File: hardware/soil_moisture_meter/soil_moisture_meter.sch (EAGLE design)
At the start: 16 parts, among them IC1 MEGA328, IC2 RFM12, IC3 74HC14D

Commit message: Remove battery measurement resistors.
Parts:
- removed R5: 100k, rcl:R-EU_R0603
- removed R6: 220R, rcl:R-EU_R0603
- R2: value 47k -> 220R
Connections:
- removed net N$1: IC1.PC1(ADC1/PCINT9), R3.2
- removed net N$14: IC1.PC0(ADC0/PCINT8), R2.2, R3.1
- net GND: no longer R2.1
- net N$10: now also R2.1; no longer R6.1
- net N$11: now also R2.2; no longer R6.2
- net N$2: now also R3.2; no longer R5.2
- net N$9: now also R3.1; no longer R5.1
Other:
- note added: "Date: 01.01.2015"
- note added: "Rev 1.1"
- note removed: "Date: 21.09.2014"
- note removed: "Rev 1.0"
- moved on the sheet: R2, R3
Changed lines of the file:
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@@
 <part name="P+2" library="supply1" deviceset="VCC" device=""/>
 <part name="P+3" library="supply1" deviceset="VCC" device=""/>
-<part name="GND3" library="supply1" deviceset="GND" device=""/>
 <part name="JP2" library="pinhead" deviceset="PINHD-1X1" device="" value="ANT"/>
 <part name="IC3" library="74xx-eu" deviceset="74*14" device="D" technology="HC"/>
-<part name="R2" library="rcl" deviceset="R-EU_" device="R0603" value="47k"/>
-<part name="R3" library="rcl" deviceset="R-EU_" device="R0603" value="100k"/>
 <part name="R1" library="rcl" deviceset="R-EU_" device="R0603" value="220R"/>
 <part name="R4" library="rcl" deviceset="R-EU_" device="R0603" value="1M"/>
-<part name="R5" library="rcl" deviceset="R-EU_" device="R0603" value="100k"/>
-<part name="R6" library="rcl" deviceset="R-EU_" device="R0603" value="220R"/>
+<part name="R3" library="rcl" deviceset="R-EU_" device="R0603" value="100k"/>
+<part name="R2" library="rcl" deviceset="R-EU_" device="R0603" value="220R"/>
 <part name="GND4" library="supply1" deviceset="GND" device=""/>
 <part name="GND5" library="supply1" deviceset="GND" device=""/>
@@
 <frame x1="-66.04" y1="-40.64" x2="154.94" y2="119.38" columns="8" rows="5" layer="97"/>
 <text x="63.5" y="104.14" size="3.81" layer="97">smarthomatic Soil Moisture Meter</text>
-<text x="114.3" y="99.06" size="2.1844" layer="97">Date: 21.09.2014</text>
-<text x="63.5" y="99.06" size="2.1844" layer="97">Rev 1.0</text>
+<text x="114.3" y="99.06" size="2.1844" layer="97">Date: 01.01.2015</text>
+<text x="63.5" y="99.06" size="2.1844" layer="97">Rev 1.1</text>
 <text x="63.5" y="93.98" size="2.1844" layer="97">Copyright (c) Uwe Freese, www.smarthomatic.org</text>
 <rectangle x1="33.02" y1="86.36" x2="38.1" y2="91.44" layer="97"/>
@@
 <instance part="P+2" gate="VCC" x="104.14" y="17.78" rot="R180"/>
 <instance part="P+3" gate="VCC" x="68.58" y="45.72" rot="R180"/>
-<instance part="GND3" gate="1" x="55.88" y="25.4"/>
 <instance part="JP2" gate="G$1" x="88.9" y="76.2"/>
 <instance part="IC3" gate="A" x="-22.86" y="76.2"/>
@@
 <instance part="IC3" gate="E" x="10.16" y="101.6"/>
 <instance part="IC3" gate="F" x="45.72" y="101.6"/>
-<instance part="R2" gate="G$1" x="55.88" y="35.56" rot="R90"/>
-<instance part="R3" gate="G$1" x="45.72" y="43.18" rot="R180"/>
 <instance part="R1" gate="G$1" x="58.42" y="5.08"/>
 <instance part="R4" gate="G$1" x="101.6" y="12.7" rot="R90"/>
-<instance part="R5" gate="G$1" x="-22.86" y="63.5"/>
-<instance part="R6" gate="G$1" x="63.5" y="71.12" rot="R270"/>
+<instance part="R3" gate="G$1" x="-22.86" y="63.5"/>
+<instance part="R2" gate="G$1" x="63.5" y="71.12" rot="R270"/>
 <instance part="GND4" gate="1" x="-38.1" y="93.98"/>
 <instance part="GND5" gate="1" x="60.96" y="12.7"/>
@@
 <junction x="127" y="-7.62"/>
 <pinref part="LED1" gate="G$1" pin="C"/>
-</segment>
-<segment>
-<pinref part="GND3" gate="1" pin="GND"/>
-<pinref part="R2" gate="G$1" pin="1"/>
-<wire x1="55.88" y1="27.94" x2="55.88" y2="30.48" width="0.1524" layer="91"/>
 </segment>
 <segment>
@@
 </segment>
 </net>
-<net name="N$14" class="0">
-<segment>
-<wire x1="55.88" y1="40.64" x2="55.88" y2="43.18" width="0.1524" layer="91"/>
-<pinref part="IC1" gate="1" pin="PC0(ADC0/PCINT8)"/>
-<wire x1="55.88" y1="43.18" x2="50.8" y2="43.18" width="0.1524" layer="91"/>
-<wire x1="35.56" y1="45.72" x2="55.88" y2="45.72" width="0.1524" layer="91"/>
-<wire x1="55.88" y1="45.72" x2="55.88" y2="43.18" width="0.1524" layer="91"/>
-<junction x="55.88" y="43.18"/>
-<pinref part="R2" gate="G$1" pin="2"/>
-<pinref part="R3" gate="G$1" pin="1"/>
-</segment>
-</net>
 <net name="N$16" class="0">
 <segment>
@@
 </segment>
 </net>
-<net name="N$1" class="0">
-<segment>
-<pinref part="IC1" gate="1" pin="PC1(ADC1/PCINT9)"/>
-<wire x1="35.56" y1="43.18" x2="40.64" y2="43.18" width="0.1524" layer="91"/>
-<pinref part="R3" gate="G$1" pin="2"/>
-</segment>
-</net>
 <net name="N$2" class="0">
 <segment>
@@
 <pinref part="IC3" gate="B" pin="I"/>
 <wire x1="-12.7" y1="76.2" x2="-5.08" y2="76.2" width="0.1524" layer="91"/>
-<pinref part="R5" gate="G$1" pin="2"/>
+<pinref part="R3" gate="G$1" pin="2"/>
 <wire x1="-5.08" y1="76.2" x2="0" y2="76.2" width="0.1524" layer="91"/>
 <wire x1="-17.78" y1="63.5" x2="-5.08" y2="63.5" width="0.1524" layer="91"/>
@@
 <wire x1="-38.1" y1="76.2" x2="-38.1" y2="63.5" width="0.1524" layer="91"/>
 <junction x="-38.1" y="76.2"/>
-<pinref part="R5" gate="G$1" pin="1"/>
+<pinref part="R3" gate="G$1" pin="1"/>
 <wire x1="-38.1" y1="63.5" x2="-27.94" y2="63.5" width="0.1524" layer="91"/>
 </segment>
@@
 <segment>
 <pinref part="IC3" gate="C" pin="O"/>
-<pinref part="R6" gate="G$1" pin="1"/>
+<pinref part="R2" gate="G$1" pin="1"/>
 <wire x1="55.88" y1="76.2" x2="63.5" y2="76.2" width="0.1524" layer="91"/>
 </segment>
@@
 <wire x1="35.56" y1="10.16" x2="63.5" y2="10.16" width="0.1524" layer="91"/>
 <wire x1="63.5" y1="10.16" x2="63.5" y2="66.04" width="0.1524" layer="91"/>
-<pinref part="R6" gate="G$1" pin="2"/>
-</segment>
-</net>
+<pinref part="R2" gate="G$1" pin="2"/>
+</segment>
+</net>

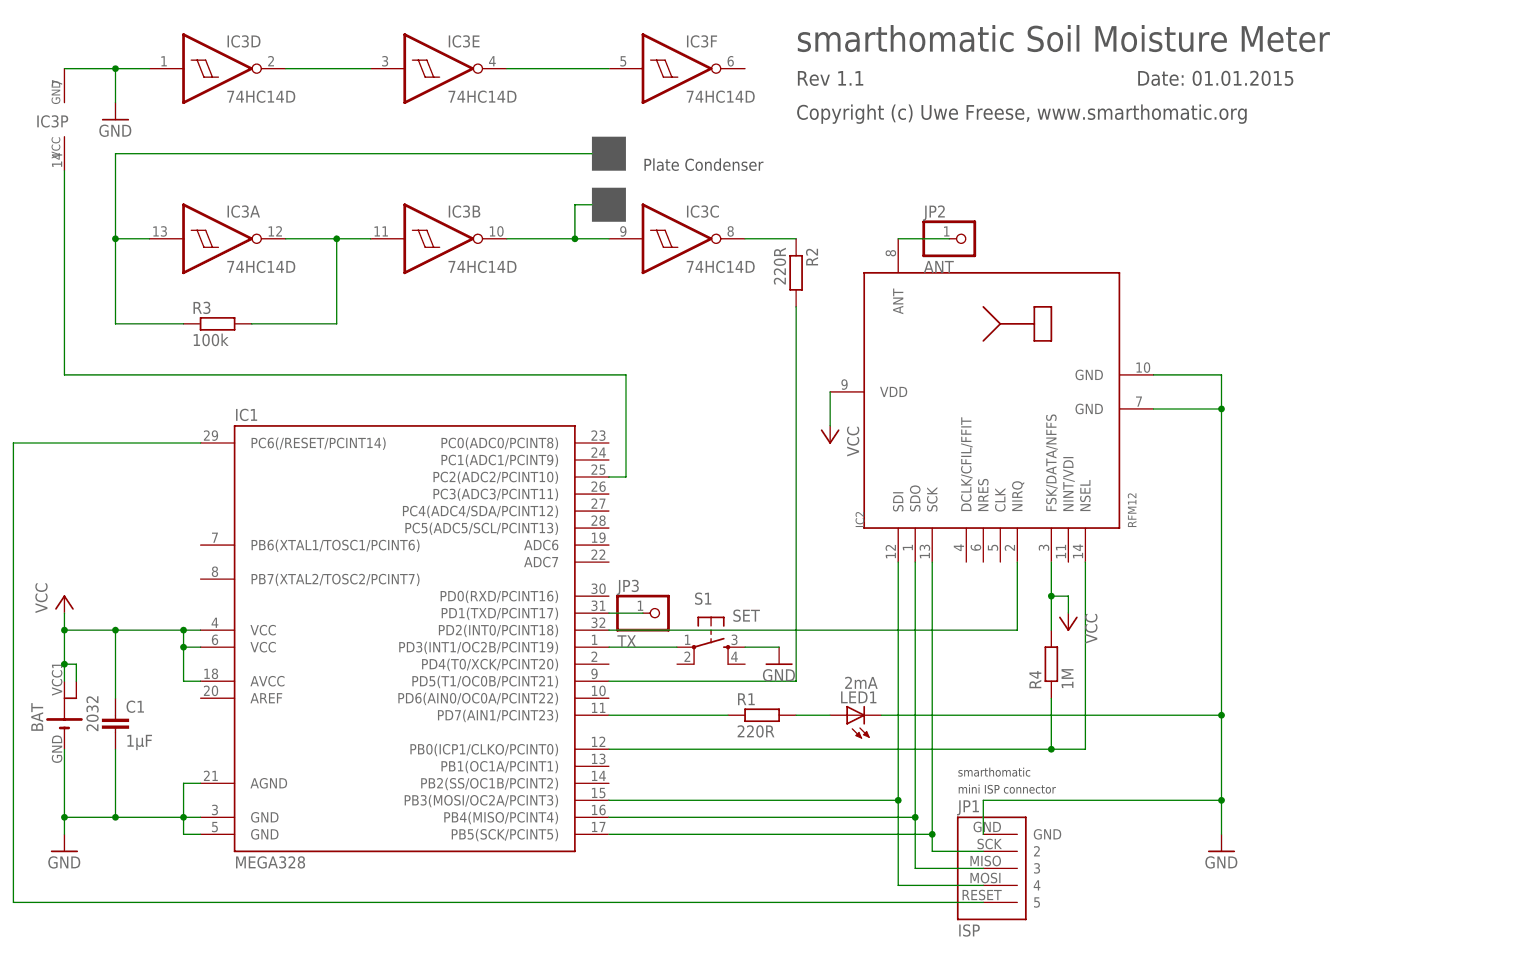
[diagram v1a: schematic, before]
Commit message: Change mini ISP connector and add 6th pin for VCC. Add solder jumper for VCC. Move ANT pin near RFM12B module. Remove resistor between 74GC14D and ATMega. Change LED resistor value.
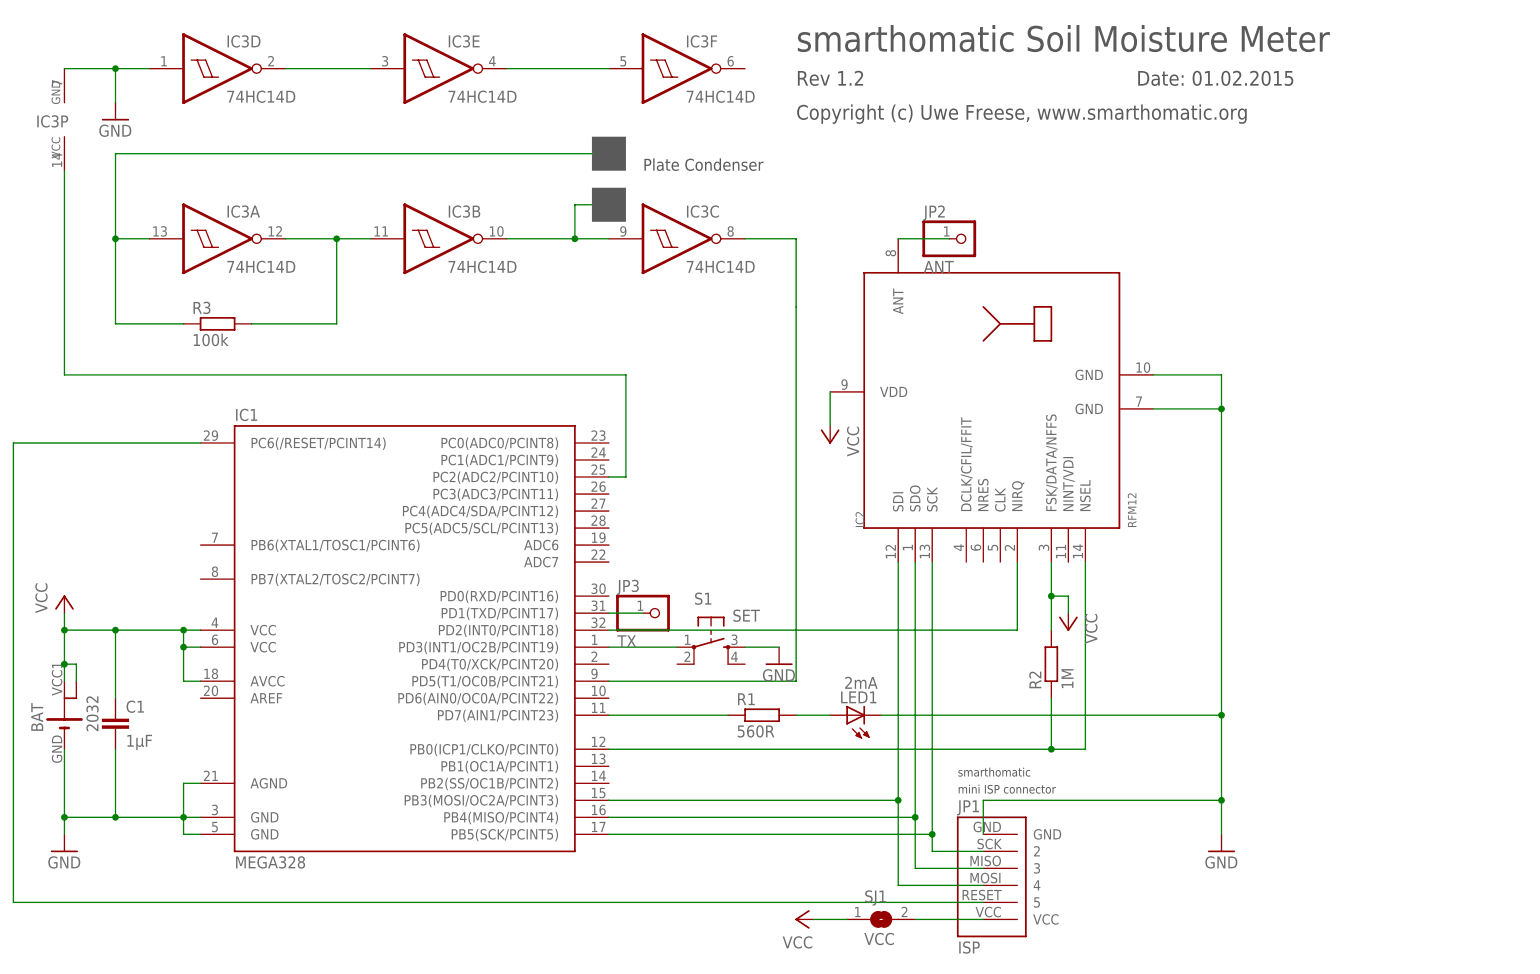
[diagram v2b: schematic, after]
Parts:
- removed R4: 1M, rcl:R-EU_R0603
- added SJ1: VCC, jumper:SJ
- R1: value 220R -> 560R
- R2: value 220R -> 1M
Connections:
- removed net N$11: IC1.PD5(T1/OC0B/PCINT21), R2.2
- new net N$1: JP1.VCC@6, SJ1.2
- net N$10: now also IC1.PD5(T1/OC0B/PCINT21); no longer R2.1
- net N$13: now also R2.1; no longer R4.1
- net VCC: now also R2.2, SJ1.1; no longer R4.2
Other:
- note added: "Date: 01.02.2015"
- note added: "Rev 1.2"
- note removed: "Date: 01.01.2015"
- note removed: "Rev 1.1"
- moved on the sheet: R2
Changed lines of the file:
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@@
 <grid distance="0.1" unitdist="inch" unit="inch" style="lines" multiple="1" display="no" altdistance="0.01" altunitdist="inch" altunit="inch"/>
 <layers>
-<layer number="1" name="Top" color="4" fill="1" visible="no" active="no"/>
-<layer number="16" name="Bottom" color="1" fill="1" visible="no" active="no"/>
-<layer number="17" name="Pads" color="2" fill="1" visible="no" active="no"/>
-<layer number="18" name="Vias" color="2" fill="1" visible="no" active="no"/>
-<layer number="19" name="Unrouted" color="6" fill="1" visible="no" active="no"/>
-<layer number="20" name="Dimension" color="15" fill="1" visible="no" active="no"/>
-<layer number="21" name="tPlace" color="7" fill="1" visible="no" active="no"/>
-<layer number="22" name="bPlace" color="7" fill="1" visible="no" active="no"/>
-<layer number="23" name="tOrigins" color="15" fill="1" visible="no" active="no"/>
-<layer number="24" name="bOrigins" color="15" fill="1" visible="no" active="no"/>
-<layer number="25" name="tNames" color="7" fill="1" visible="no" active="no"/>
-<layer number="26" name="bNames" color="7" fill="1" visible="no" active="no"/>
-<layer number="27" name="tValues" color="7" fill="1" visible="no" active="no"/>
-<layer number="28" name="bValues" color="7" fill="1" visible="no" active="no"/>
+<layer number="1" name="Top" color="4" fill="1" visible="yes" active="no"/>
+<layer number="16" name="Bottom" color="1" fill="1" visible="yes" active="no"/>
+<layer number="17" name="Pads" color="2" fill="1" visible="yes" active="no"/>
+<layer number="18" name="Vias" color="2" fill="1" visible="yes" active="no"/>
+<layer number="19" name="Unrouted" color="6" fill="1" visible="yes" active="no"/>
+<layer number="20" name="Dimension" color="15" fill="1" visible="yes" active="no"/>
+<layer number="21" name="tPlace" color="7" fill="1" visible="yes" active="no"/>
+<layer number="22" name="bPlace" color="7" fill="1" visible="yes" active="no"/>
+<layer number="23" name="tOrigins" color="15" fill="1" visible="yes" active="no"/>
+<layer number="24" name="bOrigins" color="15" fill="1" visible="yes" active="no"/>
+<layer number="25" name="tNames" color="7" fill="1" visible="yes" active="no"/>
+<layer number="26" name="bNames" color="7" fill="1" visible="yes" active="no"/>
+<layer number="27" name="tValues" color="7" fill="1" visible="yes" active="no"/>
+<layer number="28" name="bValues" color="7" fill="1" visible="yes" active="no"/>
 <layer number="29" name="tStop" color="7" fill="3" visible="no" active="no"/>
 <layer number="30" name="bStop" color="7" fill="6" visible="no" active="no"/>
@@
 <layer number="35" name="tGlue" color="7" fill="4" visible="no" active="no"/>
 <layer number="36" name="bGlue" color="7" fill="5" visible="no" active="no"/>
-<layer number="37" name="tTest" color="7" fill="1" visible="no" active="no"/>
-<layer number="38" name="bTest" color="7" fill="1" visible="no" active="no"/>
+<layer number="37" name="tTest" color="7" fill="1" visible="yes" active="no"/>
+<layer number="38" name="bTest" color="7" fill="1" visible="yes" active="no"/>
 <layer number="39" name="tKeepout" color="4" fill="11" visible="no" active="no"/>
 <layer number="40" name="bKeepout" color="1" fill="11" visible="no" active="no"/>
@@
 <layer number="44" name="Drills" color="7" fill="1" visible="no" active="no"/>
 <layer number="45" name="Holes" color="7" fill="1" visible="no" active="no"/>
-<layer number="46" name="Milling" color="3" fill="1" visible="no" active="no"/>
-<layer number="47" name="Measures" color="7" fill="1" visible="no" active="no"/>
-<layer number="48" name="Document" color="7" fill="1" visible="no" active="no"/>
-<layer number="49" name="Reference" color="7" fill="1" visible="no" active="no"/>
-<layer number="50" name="dxf" color="7" fill="1" visible="no" active="no"/>
-<layer number="51" name="tDocu" color="7" fill="1" visible="no" active="no"/>
-<layer number="52" name="bDocu" color="7" fill="1" visible="no" active="no"/>
+<layer number="46" name="Milling" color="3" fill="1" visible="yes" active="no"/>
+<layer number="47" name="Measures" color="7" fill="1" visible="yes" active="no"/>
+<layer number="48" name="Document" color="7" fill="1" visible="yes" active="no"/>
+<layer number="49" name="Reference" color="7" fill="1" visible="yes" active="no"/>
+<layer number="50" name="dxf" color="7" fill="1" visible="yes" active="no"/>
+<layer number="51" name="tDocu" color="7" fill="1" visible="yes" active="no"/>
+<layer number="52" name="bDocu" color="7" fill="1" visible="yes" active="no"/>
 <layer number="91" name="Nets" color="2" fill="1" visible="yes" active="yes"/>
 <layer number="92" name="Busses" color="1" fill="1" visible="yes" active="yes"/>
@@
 <part name="JP2" library="pinhead" deviceset="PINHD-1X1" device="" value="ANT"/>
 <part name="IC3" library="74xx-eu" deviceset="74*14" device="D" technology="HC"/>
-<part name="R1" library="rcl" deviceset="R-EU_" device="R0603" value="220R"/>
-<part name="R4" library="rcl" deviceset="R-EU_" device="R0603" value="1M"/>
+<part name="R1" library="rcl" deviceset="R-EU_" device="R0603" value="560R"/>
+<part name="R2" library="rcl" deviceset="R-EU_" device="R0603" value="1M"/>
 <part name="R3" library="rcl" deviceset="R-EU_" device="R0603" value="100k"/>
-<part name="R2" library="rcl" deviceset="R-EU_" device="R0603" value="220R"/>
 <part name="GND4" library="supply1" deviceset="GND" device=""/>
 <part name="GND5" library="supply1" deviceset="GND" device=""/>
@@
 <part name="S1" library="switch-omron-smd" deviceset="LSG" device="" value="SET"/>
 <part name="JP3" library="pinhead" deviceset="PINHD-1X1" device="" value="TX"/>
+<part name="SJ1" library="jumper" deviceset="SJ" device="" value="VCC"/>
+<part name="P+4" library="supply1" deviceset="VCC" device=""/>
 </parts>
 <sheets>
@@
 <frame x1="-66.04" y1="-40.64" x2="154.94" y2="119.38" columns="8" rows="5" layer="97"/>
 <text x="63.5" y="104.14" size="3.81" layer="97">smarthomatic Soil Moisture Meter</text>
-<text x="114.3" y="99.06" size="2.1844" layer="97">Date: 01.01.2015</text>
-<text x="63.5" y="99.06" size="2.1844" layer="97">Rev 1.1</text>
+<text x="114.3" y="99.06" size="2.1844" layer="97">Date: 01.02.2015</text>
+<text x="63.5" y="99.06" size="2.1844" layer="97">Rev 1.2</text>
 <text x="63.5" y="93.98" size="2.1844" layer="97">Copyright (c) Uwe Freese, www.smarthomatic.org</text>
 <rectangle x1="33.02" y1="86.36" x2="38.1" y2="91.44" layer="97"/>
@@
 <instance part="IC3" gate="F" x="45.72" y="101.6"/>
 <instance part="R1" gate="G$1" x="58.42" y="5.08"/>
-<instance part="R4" gate="G$1" x="101.6" y="12.7" rot="R90"/>
+<instance part="R2" gate="G$1" x="101.6" y="12.7" rot="R90"/>
 <instance part="R3" gate="G$1" x="-22.86" y="63.5"/>
-<instance part="R2" gate="G$1" x="63.5" y="71.12" rot="R270"/>
 <instance part="GND4" gate="1" x="-38.1" y="93.98"/>
 <instance part="GND5" gate="1" x="60.96" y="12.7"/>
@@
 <instance part="S1" gate="G$1" x="50.8" y="15.24" rot="R270"/>
 <instance part="JP3" gate="G$1" x="43.18" y="20.32"/>
+<instance part="SJ1" gate="1" x="76.2" y="-25.4"/>
+<instance part="P+4" gate="VCC" x="63.5" y="-25.4" rot="R90"/>
 </instances>
 <busses>
@@
 <wire x1="101.6" y1="27.94" x2="101.6" y2="22.86" width="0.1524" layer="91"/>
 <wire x1="101.6" y1="17.78" x2="101.6" y2="22.86" width="0.1524" layer="91"/>
-<pinref part="R4" gate="G$1" pin="2"/>
+<pinref part="R2" gate="G$1" pin="2"/>
 </segment>
 <segment>
@@
 <junction x="-45.72" y="12.7"/>
 </segment>
+<segment>
+<pinref part="P+4" gate="VCC" pin="VCC"/>
+<pinref part="SJ1" gate="1" pin="1"/>
+<wire x1="66.04" y1="-25.4" x2="71.12" y2="-25.4" width="0.1524" layer="91"/>
+</segment>
 </net>
 <net name="N$3" class="0">
@@
 <wire x1="35.56" y1="0" x2="101.6" y2="0" width="0.1524" layer="91"/>
 <junction x="101.6" y="0"/>
-<pinref part="R4" gate="G$1" pin="1"/>
+<pinref part="R2" gate="G$1" pin="1"/>
 </segment>
 </net>
@@
 <segment>
 <pinref part="IC3" gate="C" pin="O"/>
-<pinref part="R2" gate="G$1" pin="1"/>
 <wire x1="55.88" y1="76.2" x2="63.5" y2="76.2" width="0.1524" layer="91"/>
-</segment>
-</net>
-<net name="N$11" class="0">
-<segment>
 <pinref part="IC1" gate="1" pin="PD5(T1/OC0B/PCINT21)"/>
 <wire x1="35.56" y1="10.16" x2="63.5" y2="10.16" width="0.1524" layer="91"/>
 <wire x1="63.5" y1="10.16" x2="63.5" y2="66.04" width="0.1524" layer="91"/>
-<pinref part="R2" gate="G$1" pin="2"/>
+<wire x1="63.5" y1="76.2" x2="63.5" y2="66.04" width="0.1524" layer="91"/>
 </segment>
 </net>
@@
 </segment>
 </net>
+<net name="N$1" class="0">
+<segment>
+<pinref part="SJ1" gate="1" pin="2"/>
+<pinref part="JP1" gate="G$1" pin="VCC@6"/>
+<wire x1="81.28" y1="-25.4" x2="91.44" y2="-25.4" width="0.1524" layer="91"/>
+</segment>
+</net>
